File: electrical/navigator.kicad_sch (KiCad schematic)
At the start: 7 parts

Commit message: Interim check-in
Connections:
- net CAN_HI_IN is gone; now on net ADSB_SERIAL_OUT: GAD29.P291_1 (CAN_HI)
- net CAN_LO_IN is gone; now on net ADSB_SERIAL_IN: GAD29.P291_2 (CAN_LO)
- net CONNEXT_SERIAL_GND is gone; now on net ADSB_SERIAL_GND: GPS175.P1751_51 (RS-232_2_GND)
- net CONNEXT_SERIAL_IN is gone; now on net ADSB_SERIAL_OUT: GPS175.P1751_30 (RS-232_2_RX)
- net CONNEXT_SERIAL_OUT is gone; now on net ADSB_SERIAL_IN: GPS175.P1751_8 (RS-232_2_TX)
- net MAPMX_SERIAL_GND is gone; now on net ADSB_SERIAL_GND: GPS175.P1751_52 (RS-232_1_GND)
- net MAPMX_SERIAL_IN is gone; now on net ADSB_SERIAL_OUT: GPS175.P1751_31 (RS-232_1_RX)
- net MAPMX_SERIAL_OUT is gone; now on net ADSB_SERIAL_IN: GPS175.P1751_9 (RS-232_1_TX)
- net ADSB_SERIAL_IN: now also GAD29.P292_11 (ARINC_RX_1B), GAD29.P292_12 (ARINC_TX_1B), GPS175.P1751_28 (ARINC_429_1_RX_B), GPS175.P1751_6 (ARINC_429_1_TX_B)
- net ADSB_SERIAL_OUT: now also GAD29.P292_23 (ARINC_RX_1A), GAD29.P292_24 (ARINC_TX_1A), GPS175.P1751_27 (ARINC_429_1_RX_A), GPS175.P1751_5 (ARINC_429_1_TX_A)

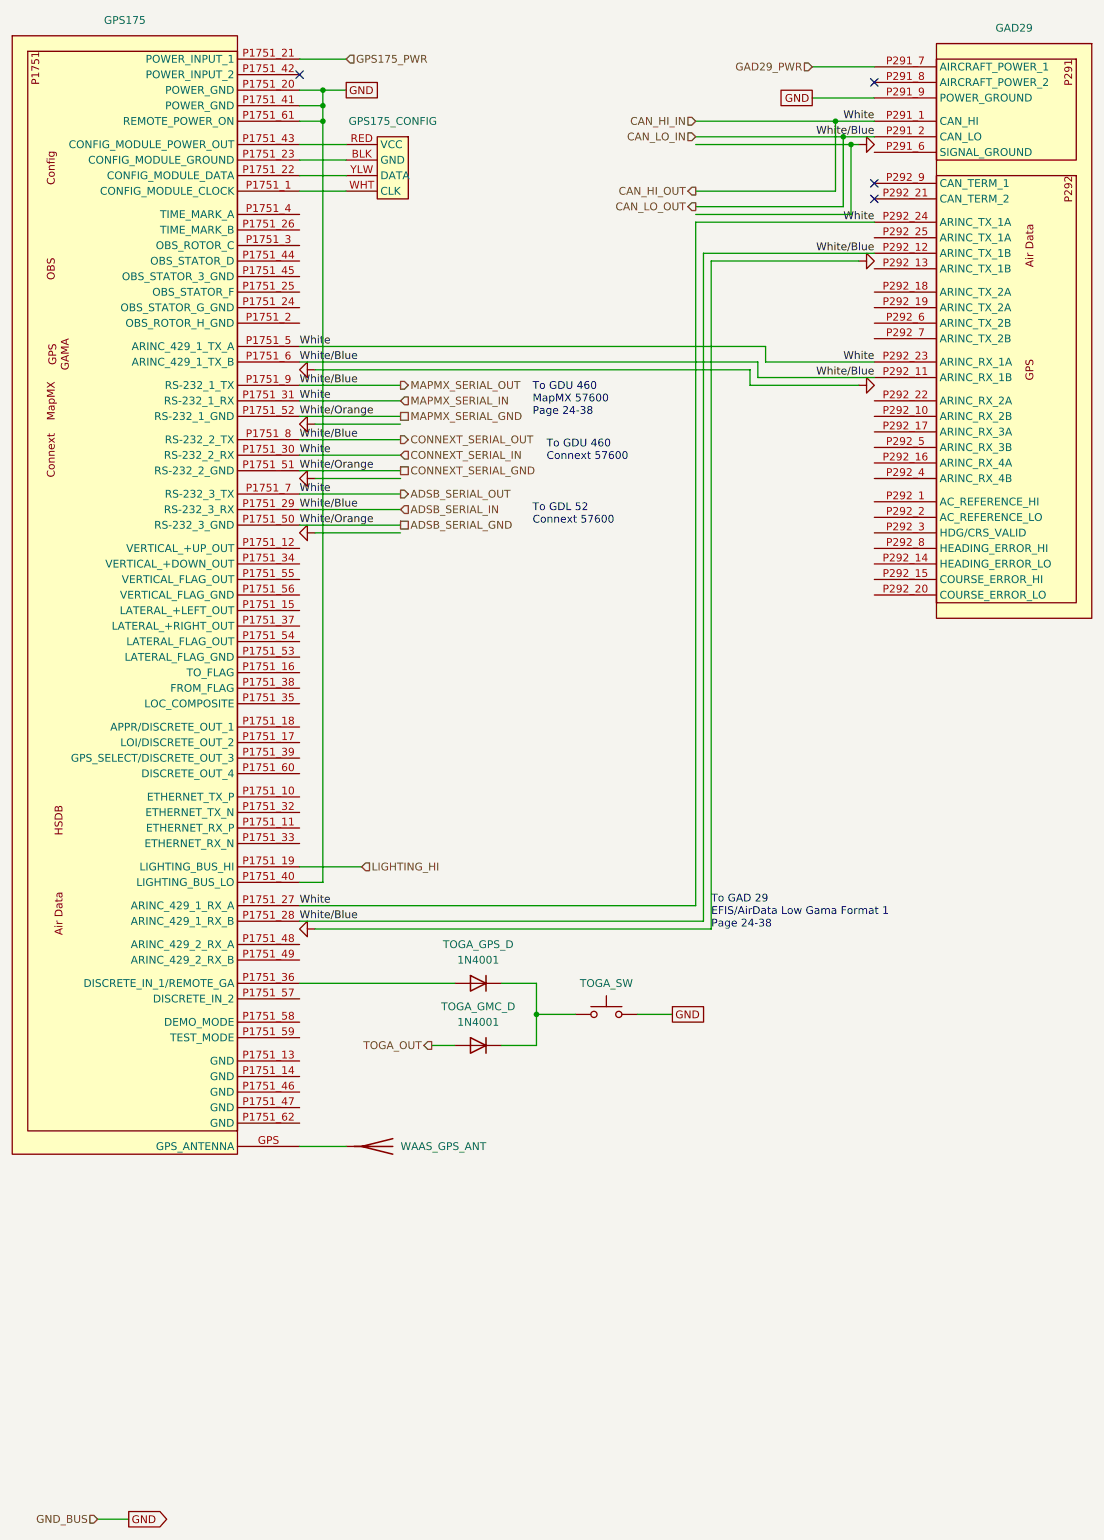
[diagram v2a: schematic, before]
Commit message: Went through and changed a lot from discussions and tradeoffs. Added GTX 330, rmemoved Connext from GDU and added to GPS 175 from GDL 52. Added relay for smoke and to not use GAD 27. Added Tach sensor for SureFly. Added carb heat. Added connectors to run panel disconnected.
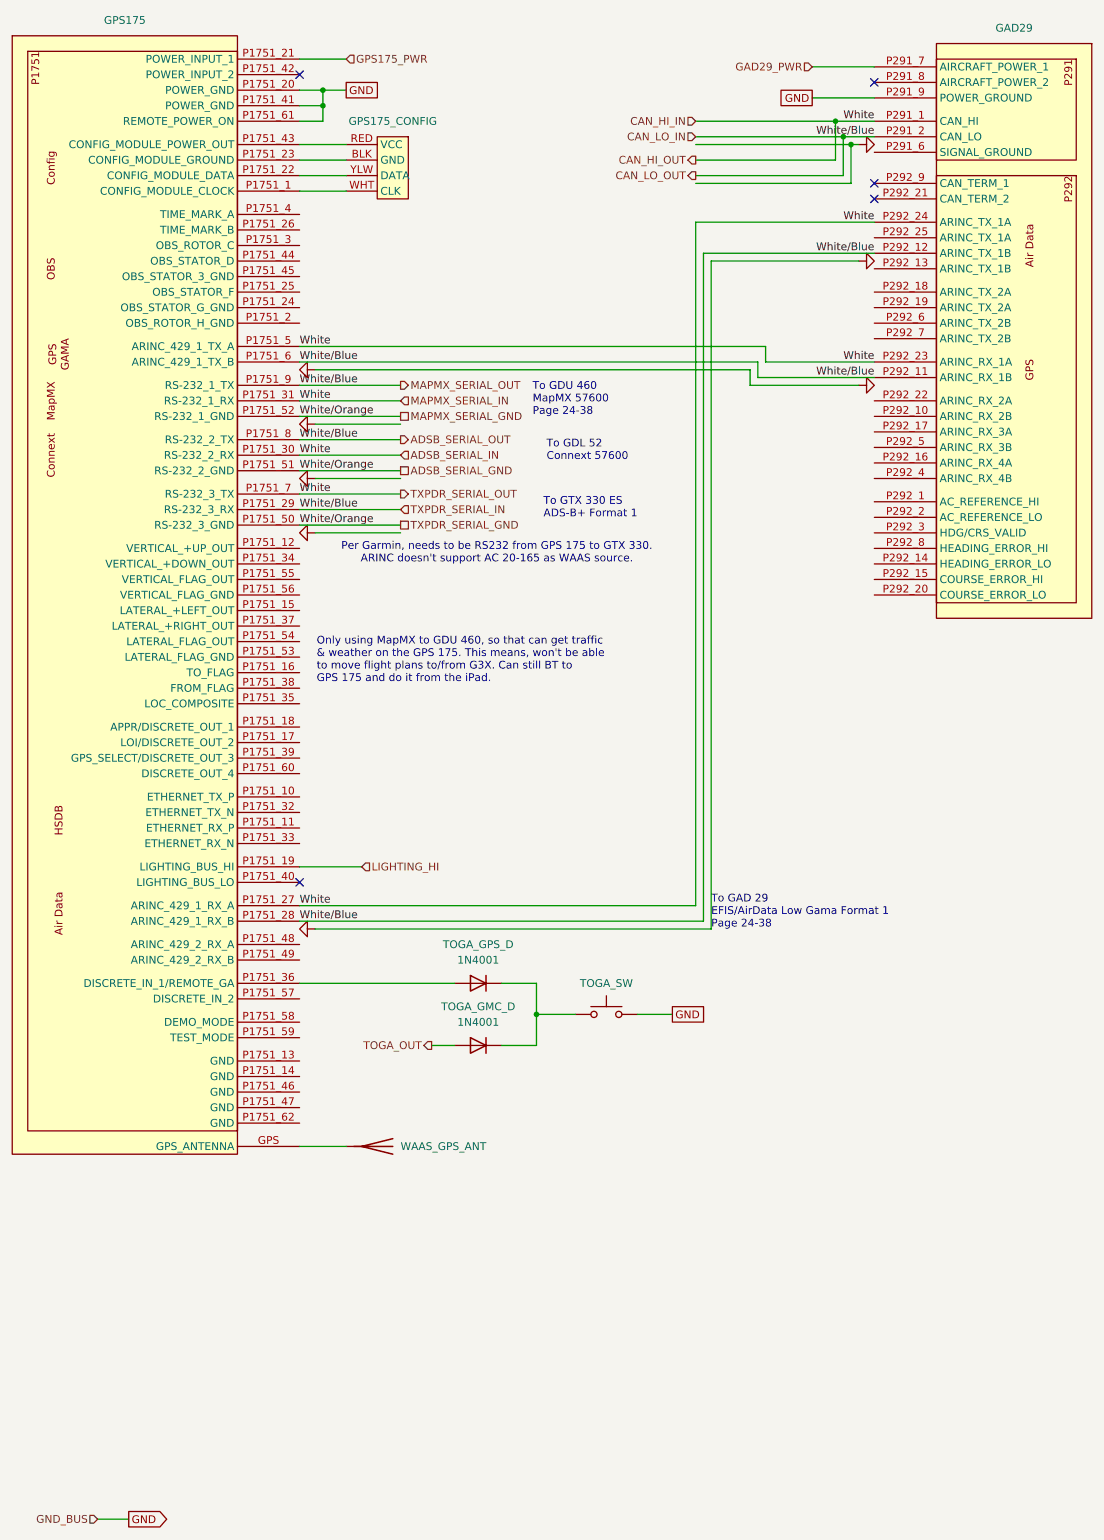
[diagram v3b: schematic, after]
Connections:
- net ADSB_SERIAL_IN: now also GAD29.P291_1 (CAN_HI), GAD29.P292_23 (ARINC_RX_1A), GAD29.P292_24 (ARINC_TX_1A), GPS175.P1751_27 (ARINC_429_1_RX_A), GPS175.P1751_30 (RS-232_2_RX), GPS175.P1751_31 (RS-232_1_RX), GPS175.P1751_5 (ARINC_429_1_TX_A), GPS175.P1751_7 (RS-232_3_TX); no longer GAD29.P291_2 (CAN_LO), GAD29.P292_11 (ARINC_RX_1B), GAD29.P292_12 (ARINC_TX_1B), GPS175.P1751_28 (ARINC_429_1_RX_B), GPS175.P1751_29 (RS-232_3_RX), GPS175.P1751_6 (ARINC_429_1_TX_B), GPS175.P1751_8 (RS-232_2_TX), GPS175.P1751_9 (RS-232_1_TX)
- net ADSB_SERIAL_OUT: now also GAD29.P291_2 (CAN_LO), GAD29.P292_11 (ARINC_RX_1B), GAD29.P292_12 (ARINC_TX_1B), GPS175.P1751_28 (ARINC_429_1_RX_B), GPS175.P1751_29 (RS-232_3_RX), GPS175.P1751_6 (ARINC_429_1_TX_B), GPS175.P1751_8 (RS-232_2_TX), GPS175.P1751_9 (RS-232_1_TX); no longer GAD29.P291_1 (CAN_HI), GAD29.P292_23 (ARINC_RX_1A), GAD29.P292_24 (ARINC_TX_1A), GPS175.P1751_27 (ARINC_429_1_RX_A), GPS175.P1751_30 (RS-232_2_RX), GPS175.P1751_31 (RS-232_1_RX), GPS175.P1751_5 (ARINC_429_1_TX_A), GPS175.P1751_7 (RS-232_3_TX)
- net GND: no longer GPS175.P1751_40 (LIGHTING_BUS_LO)
- no-connect marks 4 -> 5
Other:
- note added: "Only using MapMX to GDU 460, so that can get traffic & weather on the GPS 175. This means, won't be able to move flight plans to/from G3X. Can still BT to GPS 175 and do it from the iPad."
- note added: "Per Garmin, needs to be RS232 from GPS 175 to GTX 330. ARINC doesn't support AC 20-165 as WAAS source."
- note added: "To GTX 330 ES ADS-B+ Format 1"
- note removed: "To GDU 460 Connext 57600"
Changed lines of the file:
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@@
 	(paper "A" portrait)
 	(title_block
-		(date "2025-11-19")
-		(rev "1.1")
+		(date "2025-12-24")
+		(rev "1.2")
 		(company "N877RV")
 	)
@@
 		)
 	)
-	(text "To GDU 460\nConnext 57600"
+	(text "To GDL 52\nConnext 57600"
 		(exclude_from_sim no)
 		(at 105.156 87.376 0)
@@
 		)
 	)
-	(text "To GDL 52\nConnext 57600"
+	(text "To GTX 330 ES\nADS-B+ Format 1"
 		(exclude_from_sim no)
-		(at 102.87 97.79 0)
-		(effects
-			(font
-				(size 1.27 1.27)
-			)
-			(justify left bottom)
+		(at 104.648 94.996 0)
+		(effects
+			(font
+				(size 1.27 1.27)
+			)
+			(justify left)
+		)
+	)
+	(text "Per Garmin, needs to be RS232 from GPS 175 to GTX 330.\nARINC doesn't support AC 20-165 as WAAS source."
+		(exclude_from_sim no)
+		(at 97.028 102.362 0)
+		(effects
+			(font
+				(size 1.27 1.27)
+			)
 		)
 	)
@@
 			)
 			(justify left bottom)
+		)
+	)
+	(text "Only using MapMX to GDU 460, so that can get traffic\n& weather on the GPS 175. This means, won't be able\nto move flight plans to/from G3X. Can still BT to\nGPS 175 and do it from the iPad."
+		(exclude_from_sim no)
+		(at 67.564 119.888 0)
+		(effects
+			(font
+				(size 1.27 1.27)
+			)
+			(justify left)
 		)
 	)
@@
 	)
 	(junction
-		(at 68.58 31.75)
-		(diameter 0)
-		(color 0 0 0 0)
-	)
-	(junction
 		(at 152.4 31.75)
 		(diameter 0)
@@
 	)
 	(no_connect
+		(at 64.77 156.21)
+	)
+	(no_connect
 		(at 158.75 41.91)
 	)
@@
 	(wire
 		(pts
-			(xy 64.77 156.21) (xy 68.58 156.21)
-		)
-		(stroke
-			(width 0)
-			(type default)
-		)
-	)
-	(wire
-		(pts
 			(xy 64.77 97.79) (xy 81.28 97.79)
 		)
@@
 	(wire
 		(pts
-			(xy 154.94 35.56) (xy 154.94 46.99)
+			(xy 154.94 35.56) (xy 154.94 41.91)
 		)
 		(stroke
@@
 	(wire
 		(pts
-			(xy 129.54 43.18) (xy 152.4 43.18)
+			(xy 129.54 38.1) (xy 152.4 38.1)
 		)
 		(stroke
@@
 	(wire
 		(pts
-			(xy 68.58 156.21) (xy 68.58 31.75)
-		)
-		(stroke
-			(width 0)
-			(type default)
-		)
-	)
-	(wire
-		(pts
 			(xy 64.77 68.58) (xy 140.97 68.58)
 		)
@@
 	(wire
 		(pts
-			(xy 129.54 45.72) (xy 153.67 45.72)
+			(xy 129.54 40.64) (xy 153.67 40.64)
 		)
 		(stroke
@@
 	(wire
 		(pts
-			(xy 152.4 43.18) (xy 152.4 31.75)
+			(xy 152.4 38.1) (xy 152.4 31.75)
 		)
 		(stroke
@@
 	(wire
 		(pts
-			(xy 153.67 45.72) (xy 153.67 34.29)
+			(xy 153.67 40.64) (xy 153.67 34.29)
 		)
 		(stroke
@@
 	(wire
 		(pts
-			(xy 129.54 46.99) (xy 154.94 46.99)
+			(xy 129.54 41.91) (xy 154.94 41.91)
 		)
 		(stroke
@@
 		)
 	)
-	(hierarchical_label "ADSB_SERIAL_GND"
+	(hierarchical_label "TXPDR_SERIAL_GND"
 		(shape passive)
 		(at 81.28 97.79 0)
@@
 		)
 	)
-	(hierarchical_label "CONNEXT_SERIAL_OUT"
+	(hierarchical_label "ADSB_SERIAL_OUT"
 		(shape output)
 		(at 81.28 83.82 0)
@@
 	(hierarchical_label "CAN_LO_OUT"
 		(shape output)
-		(at 129.54 45.72 180)
+		(at 129.54 40.64 180)
 		(effects
 			(font
@@
 	(hierarchical_label "CAN_HI_OUT"
 		(shape output)
-		(at 129.54 43.18 180)
+		(at 129.54 38.1 180)
 		(effects
 			(font
@@
 		)
 	)
-	(hierarchical_label "ADSB_SERIAL_OUT"
+	(hierarchical_label "TXPDR_SERIAL_OUT"
 		(shape output)
 		(at 81.28 92.71 0)
@@
 		)
 	)
-	(hierarchical_label "ADSB_SERIAL_IN"
+	(hierarchical_label "TXPDR_SERIAL_IN"
 		(shape input)
 		(at 81.28 95.25 0)
@@
 		)
 	)
-	(hierarchical_label "CONNEXT_SERIAL_GND"
+	(hierarchical_label "ADSB_SERIAL_GND"
 		(shape passive)
 		(at 81.28 88.9 0)
@@
 		)
 	)
-	(hierarchical_label "CONNEXT_SERIAL_IN"
+	(hierarchical_label "ADSB_SERIAL_IN"
 		(shape input)
 		(at 81.28 86.36 0)

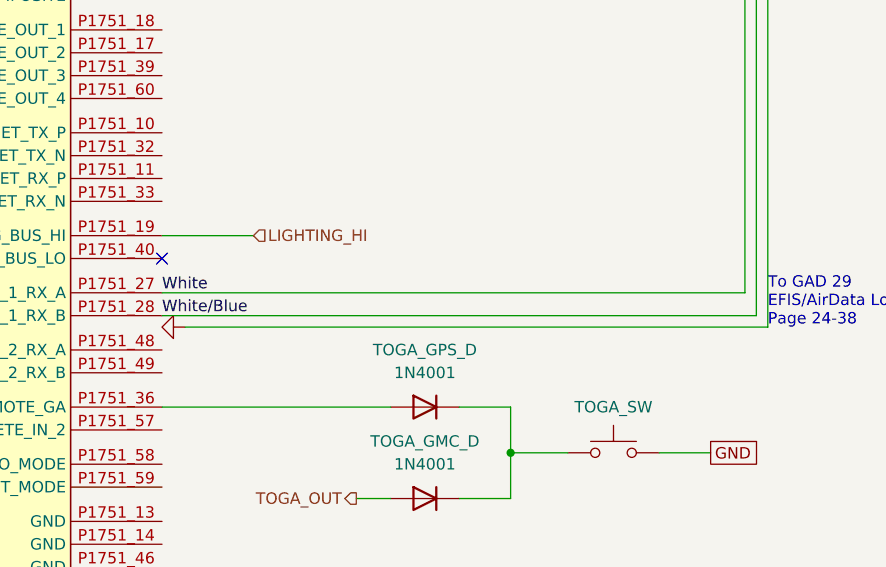
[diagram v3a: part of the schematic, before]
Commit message: Fixed can hi pin on GTR 20. Changed how ACX-BT wires with low vs. shield. Added pitch trim colors. Removed pitch trim ground going to flaps ground. Removed extra connector on GDL 52 and changed to 4 wire shielded instead of two 2 wire shielded.
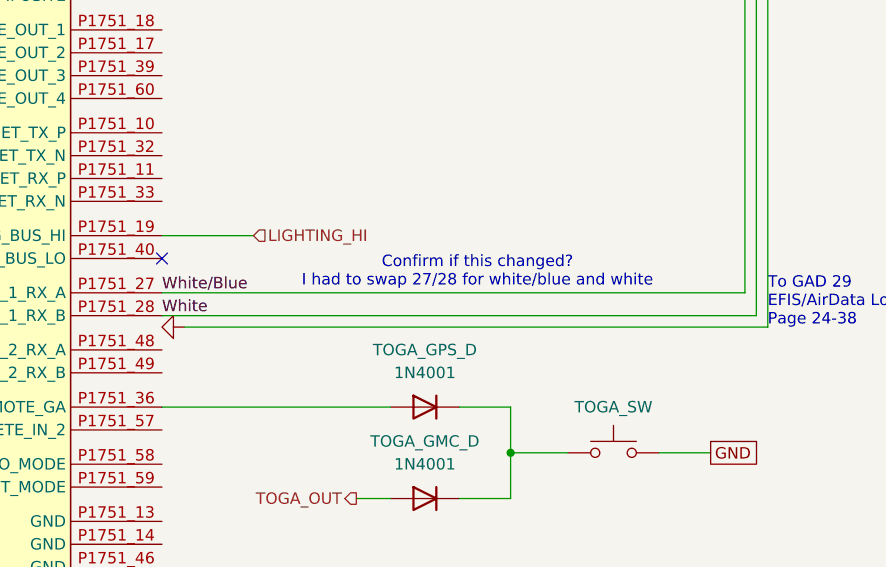
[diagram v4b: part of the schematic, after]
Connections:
- net ADSB_SERIAL_OUT is gone; now on net ADSB_SERIAL_IN: GAD29.P291_2 (CAN_LO), GAD29.P292_11 (ARINC_RX_1B), GAD29.P292_12 (ARINC_TX_1B), GPS175.P1751_28 (ARINC_429_1_RX_B), GPS175.P1751_29 (RS-232_3_RX), GPS175.P1751_6 (ARINC_429_1_TX_B), GPS175.P1751_8 (RS-232_2_TX), GPS175.P1751_9 (RS-232_1_TX)
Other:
- note added: "Confirm if this changed? I had to swap 27/28 for white/blue and white"
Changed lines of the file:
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@@
+		)
+	)
+	(text "Confirm if this changed?\nI had to swap 27/28 for white/blue and white"
+		(exclude_from_sim no)
+		(at 99.822 157.734 0)
+		(effects
+			(font
+				(size 1.27 1.27)
+			)
 		)
 	)
@@
 		)
 	)
-	(label "White{slash}Blue"
+	(label "White"
 		(at 64.77 162.56 0)
 		(effects
@@
 		)
 	)
-	(label "White"
+	(label "White{slash}Blue"
 		(at 64.77 160.02 0)
 		(effects
